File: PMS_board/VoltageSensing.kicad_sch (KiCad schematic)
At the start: 29 parts, among them U3 Opamp_Quad, U4 Opamp_Quad, U5 Opamp_Quad

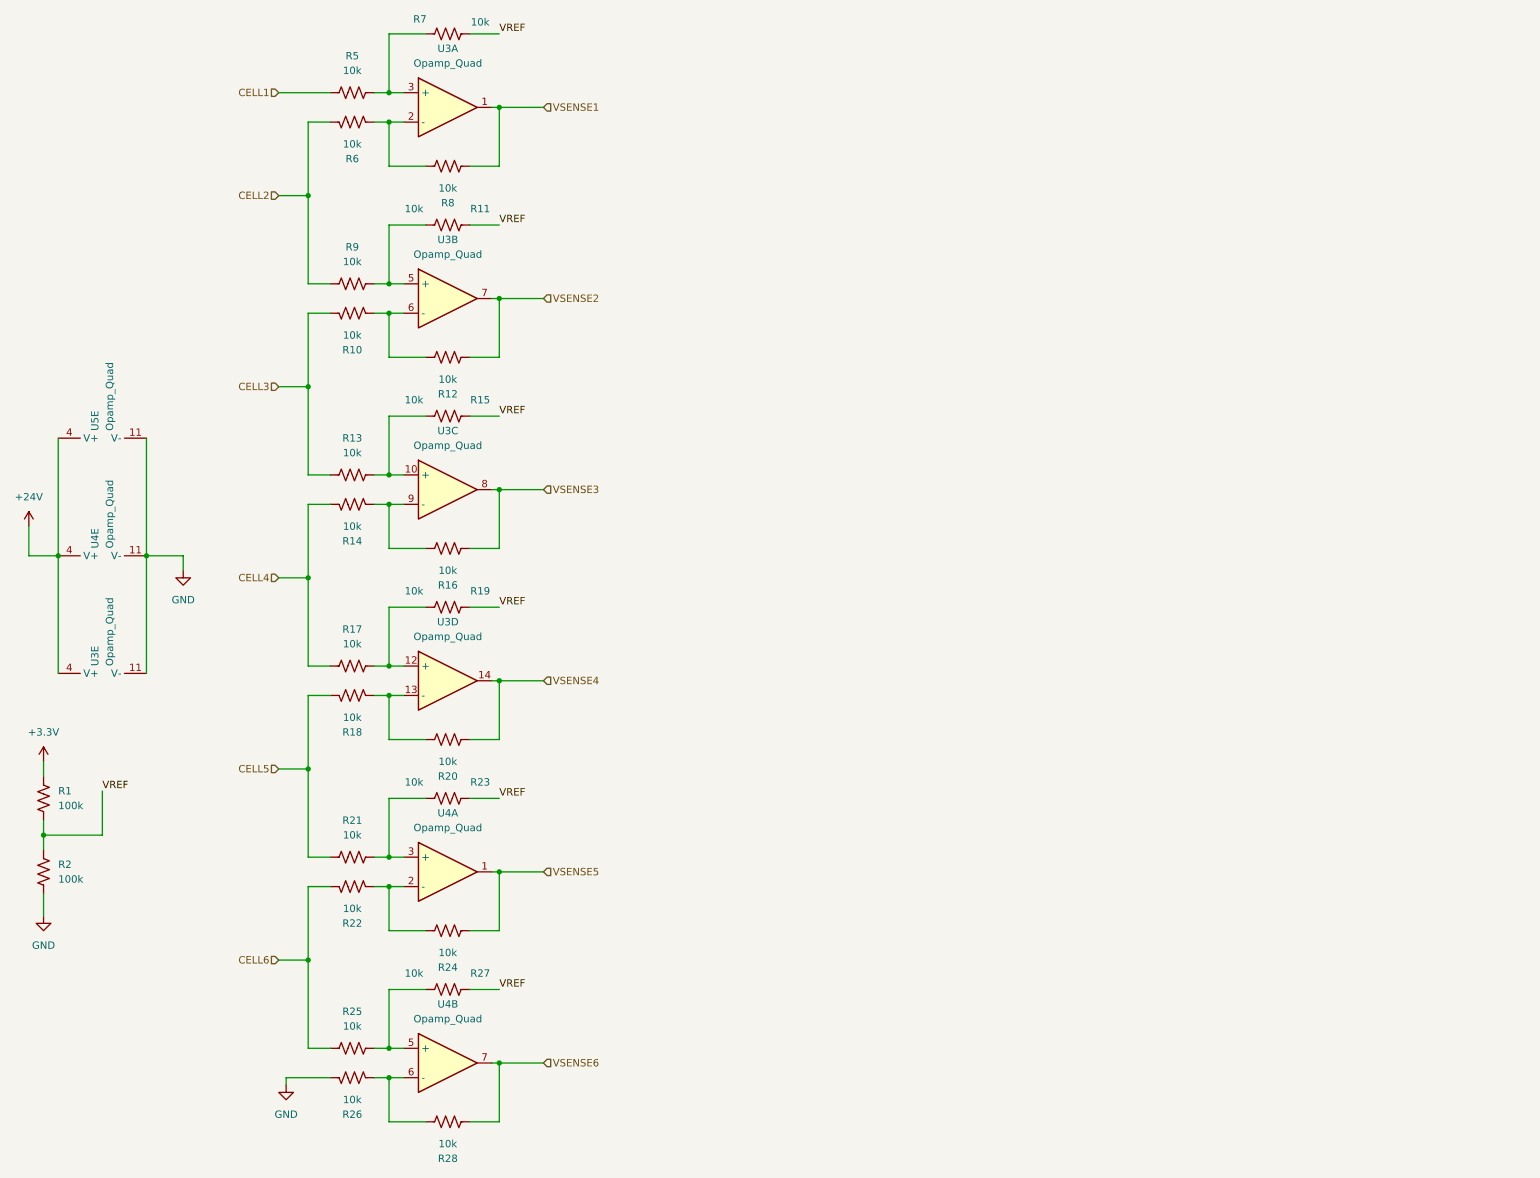
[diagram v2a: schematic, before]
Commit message: Finish Schematic
There's definitely stuff I missed, but I'm tired so we can review later. For my members to keep track of things, these are the changes/last minute additions I ran out of time to teach:
- brake chopper circuitry & reverse voltage protection for aux & motor rails
- microcontroller pinnouts
- net connections between sheets
- voltage resistors & system voltage measurements
- cell sense connectors & switch
- ADC routing
Please Please PLEASE ask questions about these additions. I don't want you guys to feel like you don't own this schematic, and I'm sorry I had to take away some of these designs to finish early. I definitely left too much on your plate to get everything perfect, which is my bad. I will happily walk through each and every circuit and help explain each part so you can better know your project when we get to reviewing and debugging later down the line.
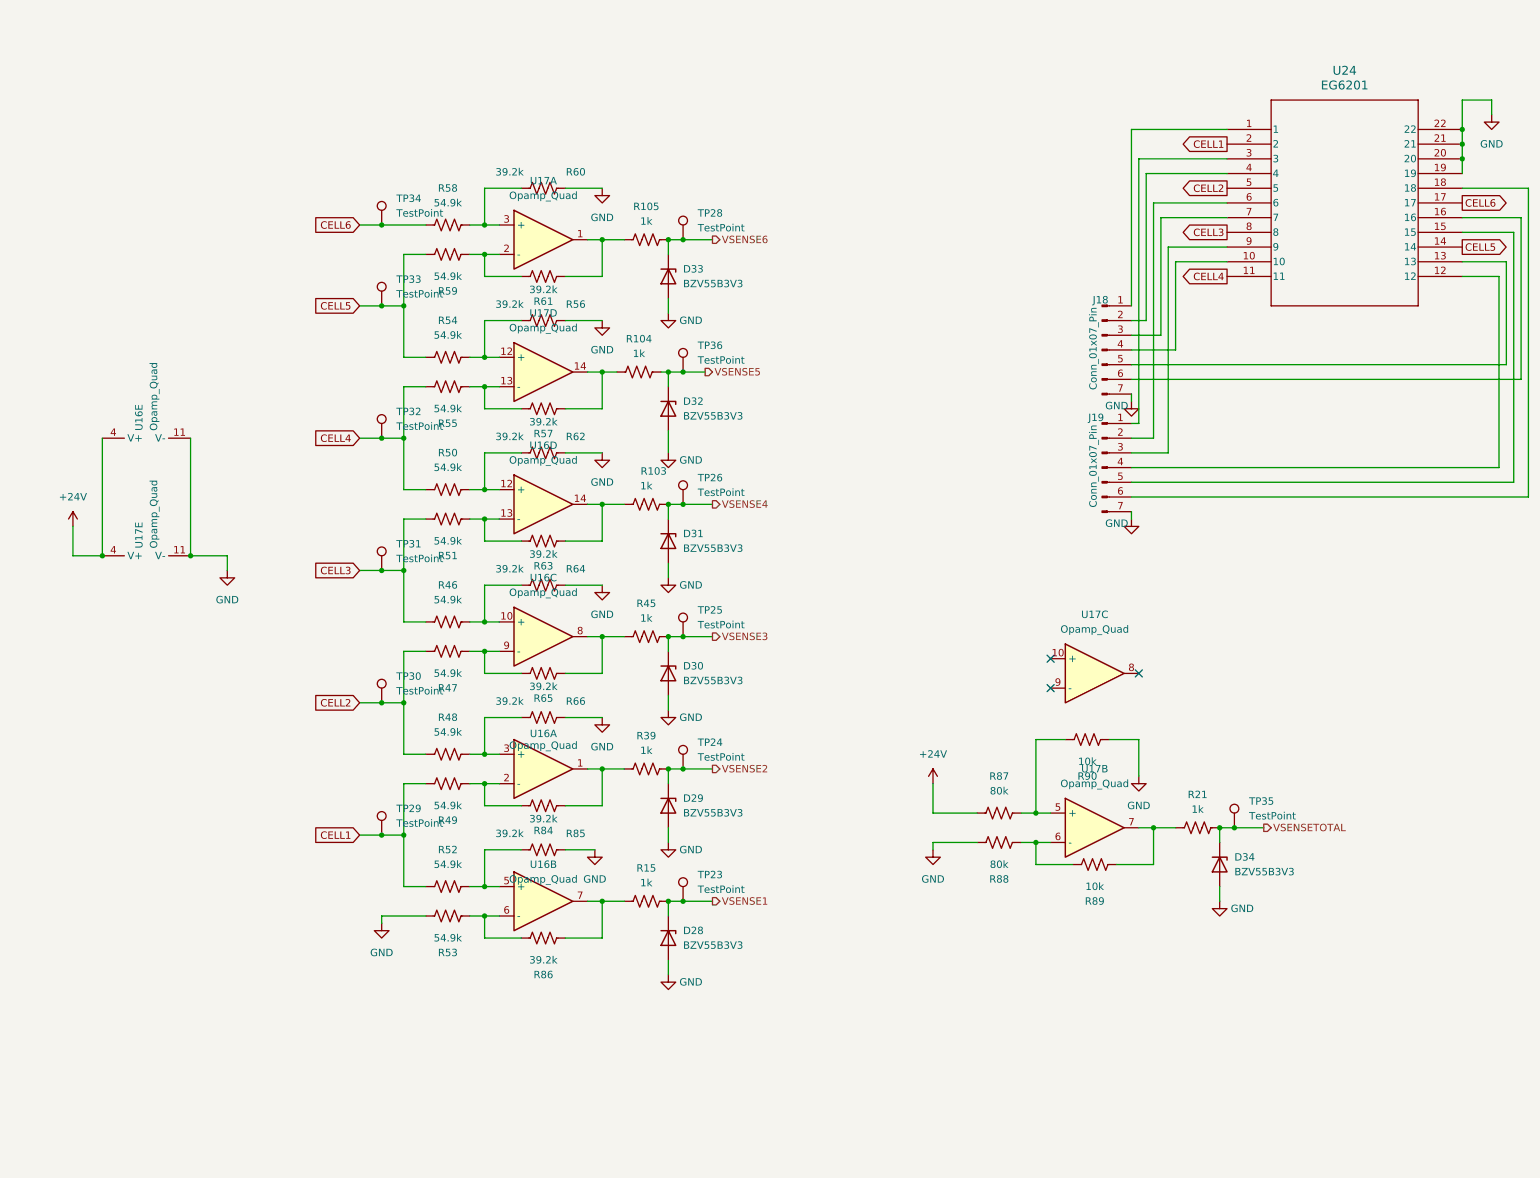
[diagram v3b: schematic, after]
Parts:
- removed R1, R2: 100k, symbol Device:R_US
- removed R10, R11, R12, R13, R14, R16, R17, R18, R19, R20, R22, R23, R24, R25, R26, R27, R28, R5, R6, R7, R8, R9: 10k, symbol Device:R_US
- removed U3: Opamp_Quad, Package_TO_SOT_SMD:SOT-353_SC-70-5, symbol Amplifier_Operational:Opamp_Quad
- removed U4, U5: Opamp_Quad, symbol Amplifier_Operational:Opamp_Quad
- added D28, D29, D30, D31, D32, D33, D34: BZV55B3V3, Diode_SMD:D_MiniMELF, symbol Diode:BZV55B3V3
- added J18, J19: Conn_01x07_Pin, Converter_DCDC:Converter_DCDC_Cyntec_MUN12AD01-SH, symbol Connector:Conn_01x07_Pin
- added R103, R104, R105, R39, R45: 1k, Resistor_SMD:R_0603_1608Metric_Pad0.98x0.95mm_HandSolder, symbol Device:R_US
- added R46, R47, R48, R49, R50, R51, R52, R53, R54, R55, R58, R59: 54.9k, symbol Device:R_US
- added R56, R57, R60, R61, R62, R63, R64, R65, R66, R84, R85, R86: 39.2k, symbol Device:R_US
- added R87, R88: 80k, symbol Device:R_US
- added R89, R90: 10k, symbol Device:R_US
- added TP23, TP24, TP25, TP26, TP28, TP29, TP30, TP31, TP32, TP33, TP34, TP35, TP36: TestPoint, TestPoint:TestPoint_Pad_D1.0mm, symbol Connector:TestPoint
- added U16, U17: Opamp_Quad, symbol Amplifier_Operational:Opamp_Quad
- added U24: EG6201, DIP_G6201_EWI, symbol EG6201:EG6201
- R15, R21: value 10k -> 1k; footprint (none) -> Resistor_SMD:R_0603_1608Metric_Pad0.98x0.95mm_HandSolder
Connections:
- net +24V: now also R87.1, U16.4 (V+), U17.4 (V+)
- net CELL1: now also R49.2, R52.1, TP29.1, U24.2
- net CELL2: now also R47.2, R48.1, TP30.1, U24.5
- net CELL3: now also R46.1, R51.2, TP31.1, U24.8
- net CELL4: now also R50.1, R55.2, TP32.1, U24.11
- net CELL5: now also R54.1, R59.2, TP33.1, U24.14; no longer R21.1
- net CELL6: now also R58.1, TP34.1, U24.17
- net GND: now also D28.2 (A), D29.2 (A), D30.2 (A), D31.2 (A), D32.2 (A), D33.2 (A), D34.2 (A), J18.7 (Pin_7), J19.7 (Pin_7), R53.2, R56.1, R60.1, R62.1, R64.1, R66.1, R85.1, R88.2, R90.2, U16.11 (V-), U17.11 (V-), U24.19, U24.20, U24.21, U24.22
- net VSENSE1: now also R15.2, D28.1 (K), TP23.1
- net VSENSE2: now also D29.1 (K), R39.2, TP24.1
- net VSENSE3: now also D30.1 (K), R45.2, TP25.1
- net VSENSE4: now also D31.1 (K), R103.2, TP26.1
- net VSENSE5: now also D32.1 (K), R104.2, TP36.1
- net VSENSE6: now also D33.1 (K), R105.2, TP28.1
- net VSENSETOTAL: now reaches R21.2
- net VSENSETOTAL: now also D34.1 (K), TP35.1
- net VREF: no longer names the net of R15.1
- net VREF: now also R86.2, U16.7
- new net: R48.2, R66.2, U16.3 (+)
- new net: R58.2, R60.2, U17.3 (+)
- new net: R50.2, R62.2, U16.12 (+)
- new net: J18.1 (Pin_1), U24.1
- new net: J18.4 (Pin_4), U24.10
- new net: J19.4 (Pin_4), U24.12
- new net: J18.5 (Pin_5), U24.13
- new net: J19.5 (Pin_5), U24.15
- new net: J18.6 (Pin_6), U24.16
- new net: J19.6 (Pin_6), U24.18
- new net: J19.1 (Pin_1), U24.3
- new net: J18.2 (Pin_2), U24.4
- new net: J19.2 (Pin_2), U24.6
- new net: J18.3 (Pin_3), U24.7
- new net: J19.3 (Pin_3), U24.9
- new net: R55.1, R57.1, U17.13 (-)
- new net: R59.1, R61.1, U17.2 (-)
- new net: R54.2, R56.2, U17.12 (+)
- new net: R45.1, R65.2, U16.8
- new net: R53.1, R86.1, U16.6 (-)
- new net: R51.1, R63.1, U16.13 (-)
- new net: R47.1, R65.1, U16.9 (-)
- new net: R105.1, R61.2, U17.1
- new net: R104.1, R57.2, U17.14
- new net: R87.2, R90.1, U17.5 (+)
- new net: R46.2, R64.2, U16.10 (+)
- new net: R103.1, R63.2, U16.14
- new net: R52.2, R85.2, U16.5 (+)
- new net: R49.1, R84.1, U16.2 (-)
- new net: R39.1, R84.2, U16.1
- new net: R21.1, R89.2, U17.7
- new net: R88.1, R89.1, U17.6 (-)
- no-connect marks 0 -> 3

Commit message: Add Footprints & such
whoops forgot to push yesterday teehee
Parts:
- added unit 3 of U16
- added unit 2 of U16
- added unit 2 of U17
- added unit 1 of U17
- added unit 4 of U17
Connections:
- net at R58.2, R60.2: now also U17.3 (+); no longer U17.3 (+)
- net at R55.1, R57.1: now also U17.13 (-); no longer U17.13 (-)
- net at R59.1, R61.1: now also U17.2 (-); no longer U17.2 (-)
- net at R54.2, R56.2: now also U17.12 (+); no longer U17.12 (+)
- net at R45.1, R65.2: now also U16.8; no longer U16.8
- net at R53.1, R86.1: now also U16.6 (-); no longer U16.6 (-)
- net at R47.1, R65.1: now also U16.9 (-); no longer U16.9 (-)
- net at R105.1, R61.2: now also U17.1; no longer U17.1
- net at R104.1, R57.2: now also U17.14; no longer U17.14
- net at R87.2, R90.1: now also U17.5 (+); no longer U17.5 (+)
- net at R46.2, R64.2: now also U16.10 (+); no longer U16.10 (+)
- net at R52.2, R85.2: now also U16.5 (+); no longer U16.5 (+)
- net at R21.1, R89.2: now also U17.7; no longer U17.7
- net at R88.1, R89.1: now also U17.6 (-); no longer U17.6 (-)
- net at R15.1, R86.2: now also U16.7; no longer U16.7

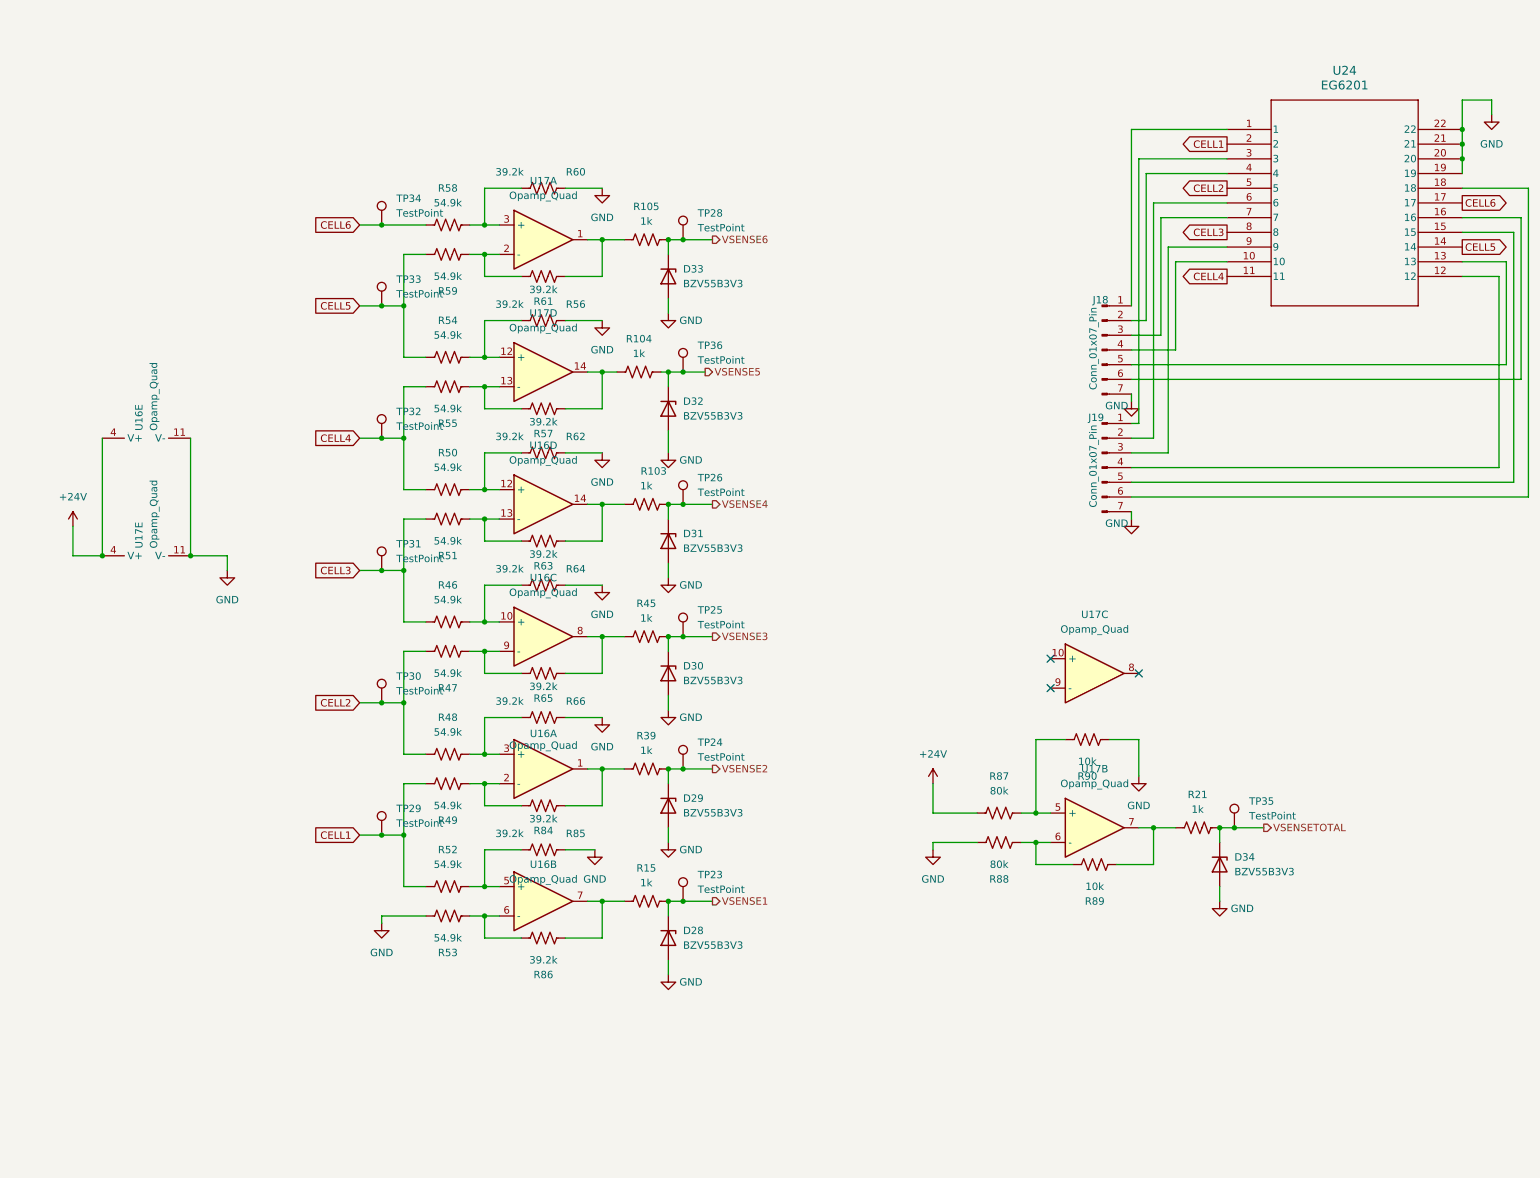
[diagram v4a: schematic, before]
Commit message: Minor component tweaks and added a seperate LED sheet
Changed component values
Added labels
Moved LEDs to it's own sheet
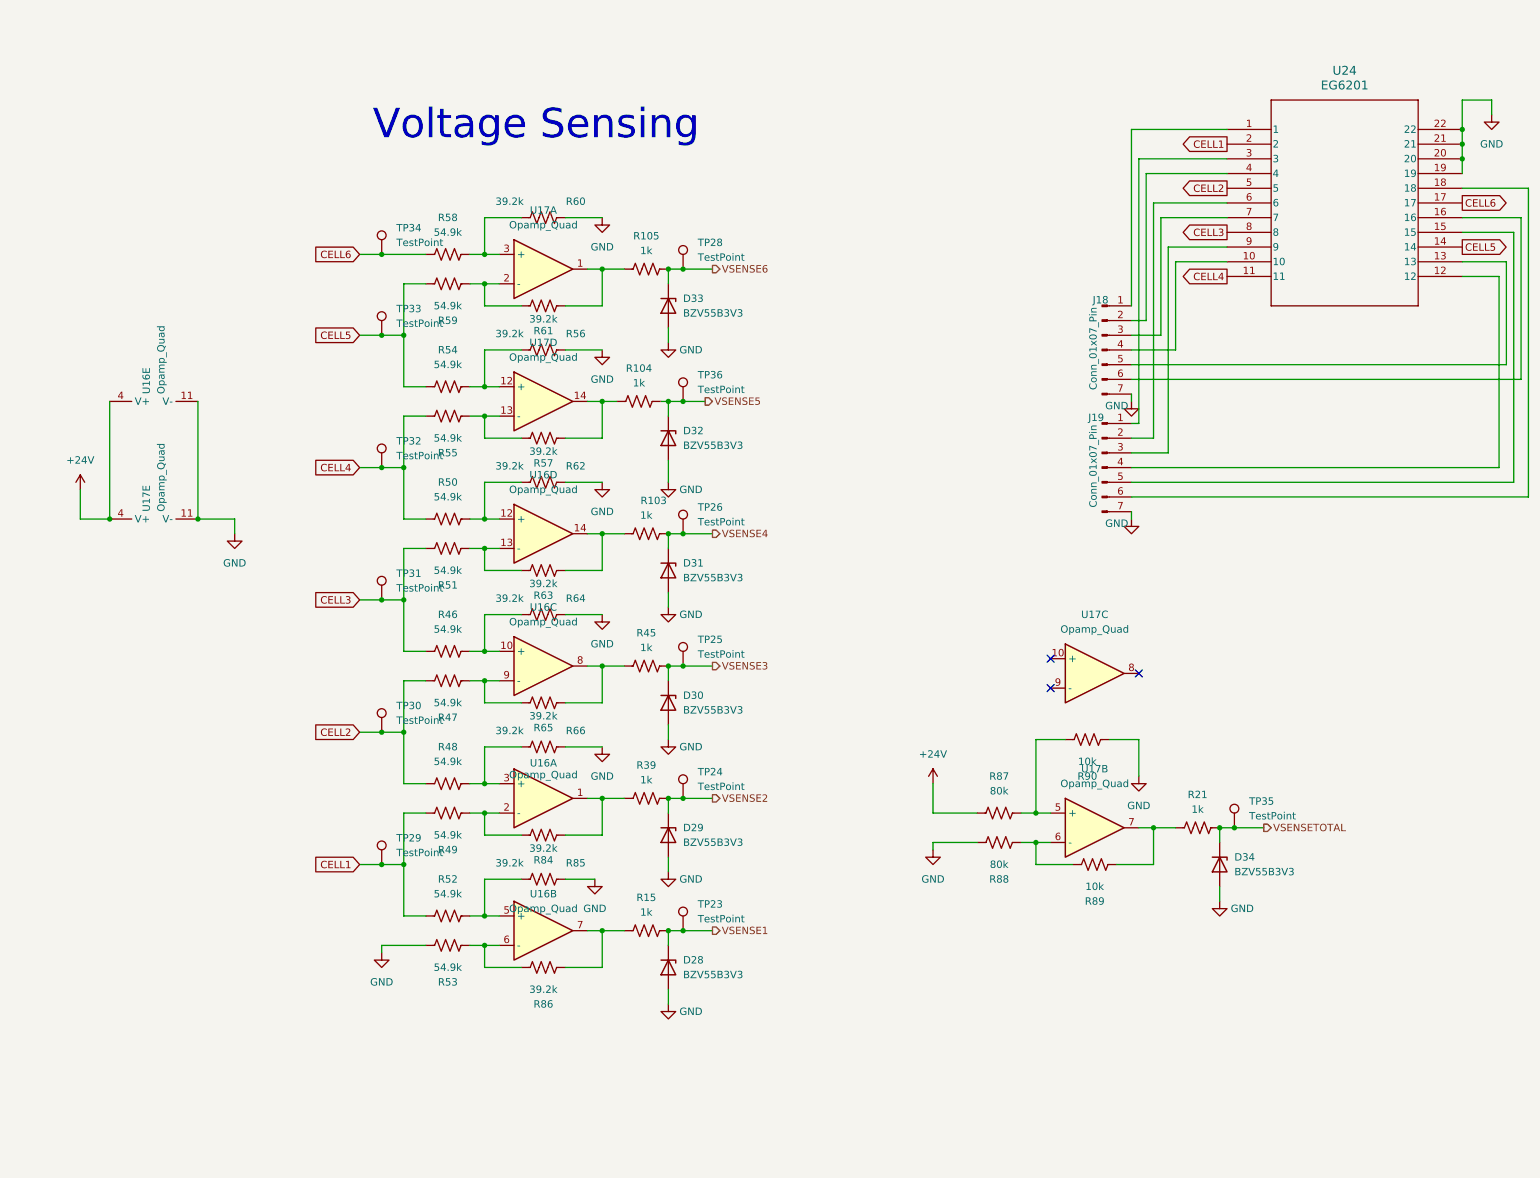
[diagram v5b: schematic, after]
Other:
- note added: "Voltage Sensing"
- moved on the sheet: D28, D29, D30, D31, D32, D33, R103, R104, R105, R15, R39, R45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
